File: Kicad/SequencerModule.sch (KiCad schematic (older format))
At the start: 13 parts, among them U1 L78L05_SOT89, U2 MCP4822, U4 TL072

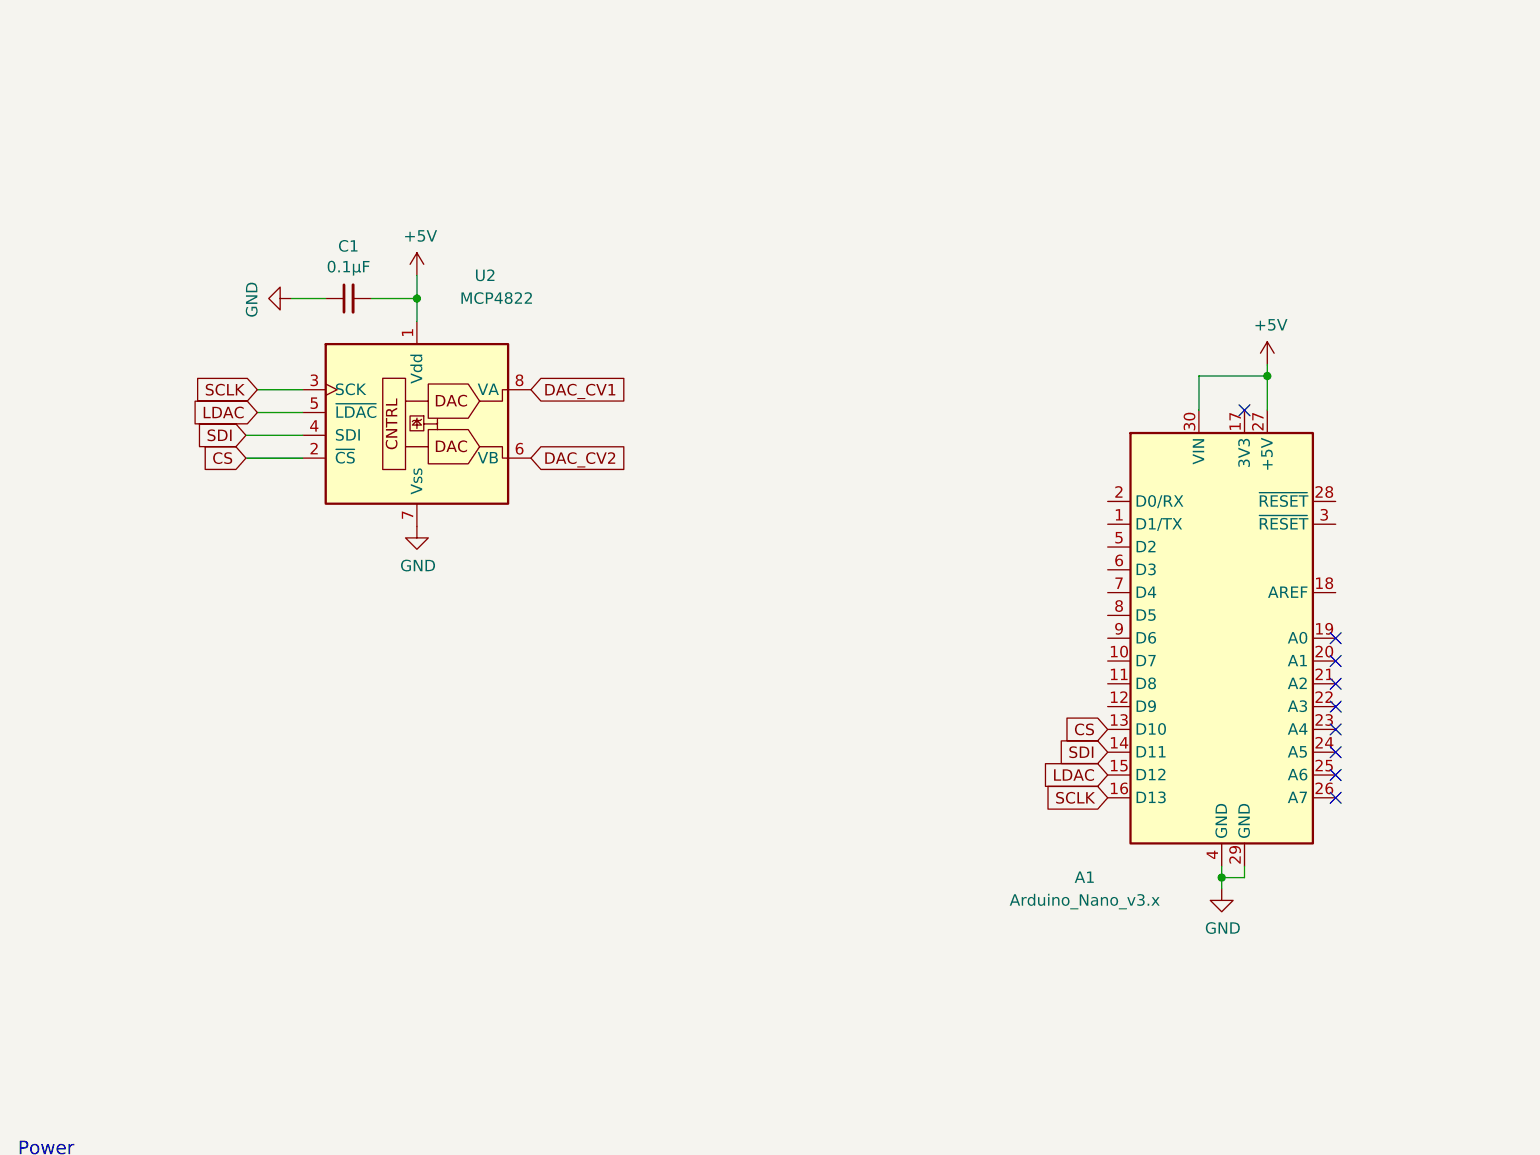
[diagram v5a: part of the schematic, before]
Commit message: switching for stm32F401, bye AtMega
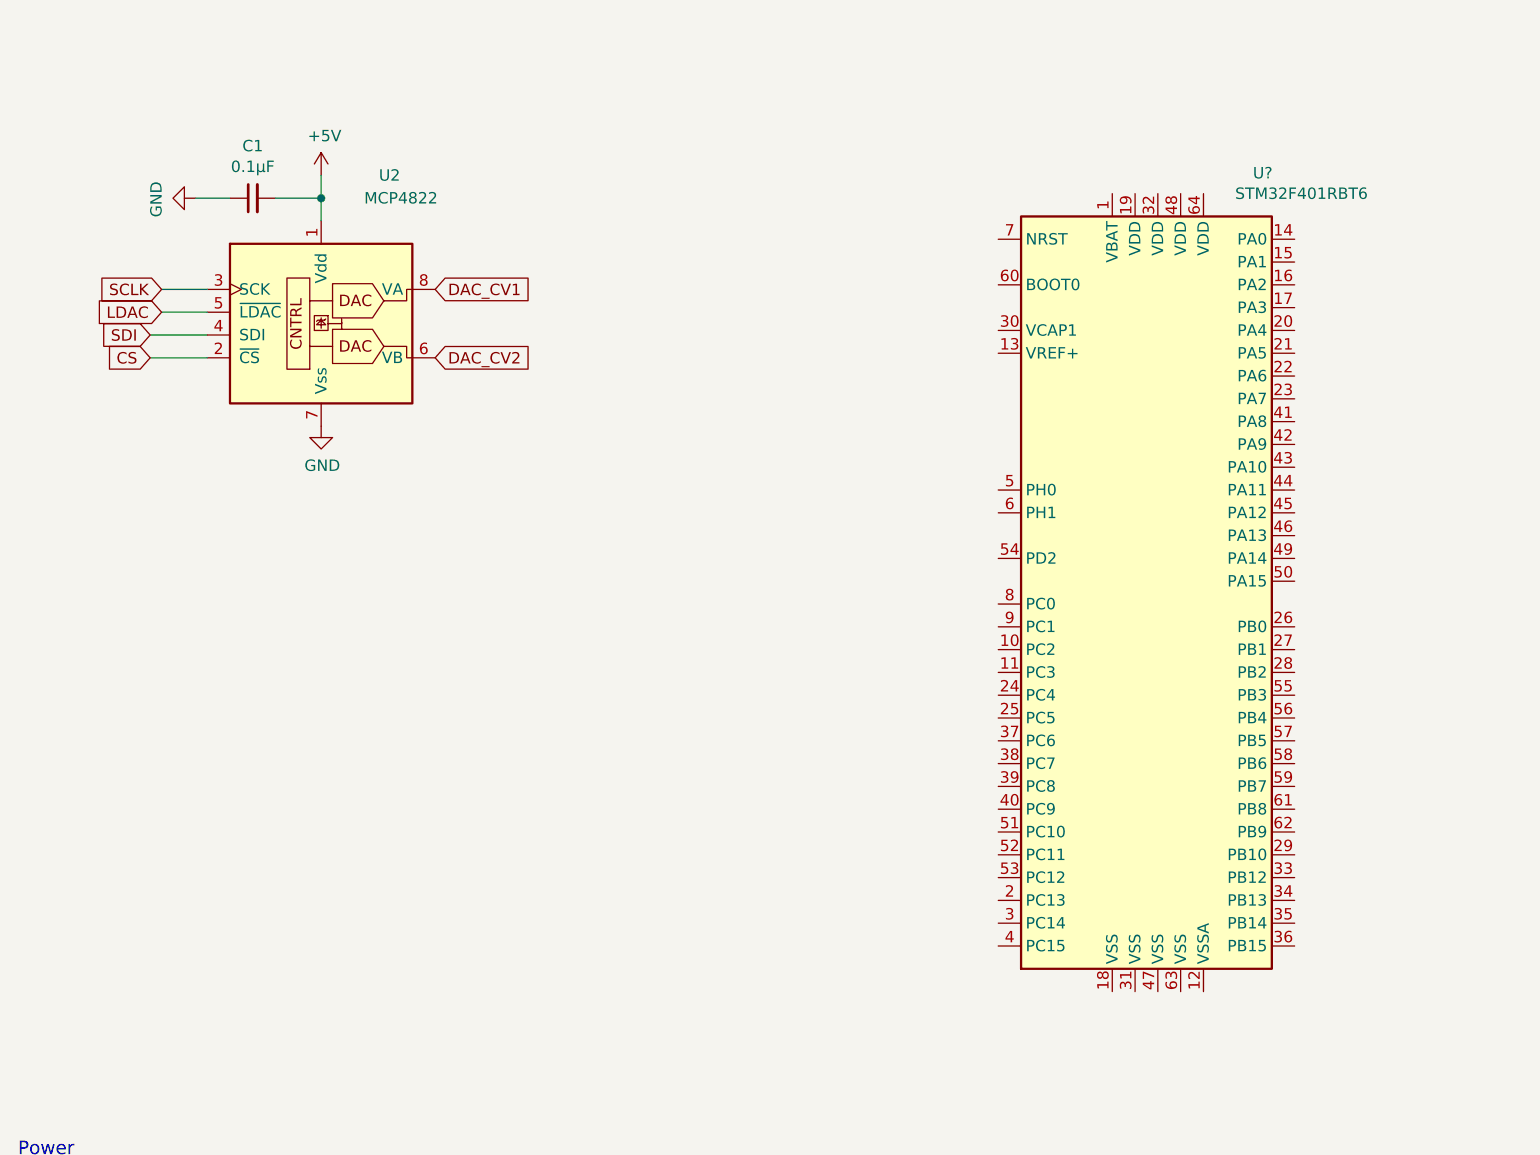
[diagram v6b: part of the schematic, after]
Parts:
- removed A1: Arduino_Nano_v3.x, Module:Arduino_Nano, symbol MCU_Module:Arduino_Nano_v3.x
- added U?: STM32F401RBT6, Package_QFP:LQFP-64_10x10mm_P0.5mm, symbol MCU_ST_STM32F4:STM32F401RBTx
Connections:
- no-connect marks 9 -> 0
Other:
- moved on the sheet: C1, U2
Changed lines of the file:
@@
 L Analog_DAC:MCP4822 U2
 U 1 1 5FAC40C6
-P 2600 2630
-F 0 "U2" H 2900 3230 50  0000 C CNN
-F 1 "MCP4822" H 2950 3130 50  0000 C CNN
-F 2 "" H 3400 2330 50  0001 C CNN
-F 3 "http://ww1.microchip.com/downloads/en/DeviceDoc/20002249B.pdf" H 3400 2330 50  0001 C CNN
-	1    2600 2630
+P 2180 2190
+F 0 "U2" H 2480 2790 50  0000 C CNN
+F 1 "MCP4822" H 2530 2690 50  0000 C CNN
+F 2 "" H 2980 1890 50  0001 C CNN
+F 3 "http://ww1.microchip.com/downloads/en/DeviceDoc/20002249B.pdf" H 2980 1890 50  0001 C CNN
+	1    2180 2190
 	1    0    0    -1
 $EndComp
@@
 L power:GND #PWR0101
 U 1 1 5FAC5967
-P 2600 3130
-F 0 "#PWR0101" H 2600 2880 50  0001 C CNN
-F 1 "GND" H 2605 2957 50  0000 C CNN
-F 2 "" H 2600 3130 50  0001 C CNN
-F 3 "" H 2600 3130 50  0001 C CNN
-	1    2600 3130
+P 2180 2690
+F 0 "#PWR0101" H 2180 2440 50  0001 C CNN
+F 1 "GND" H 2185 2517 50  0000 C CNN
+F 2 "" H 2180 2690 50  0001 C CNN
+F 3 "" H 2180 2690 50  0001 C CNN
+	1    2180 2690
 	1    0    0    -1
 $EndComp
@@
 L Device:C_Small C1
 U 1 1 5FAC8AF5
-P 2300 2130
-F 0 "C1" V 2529 2130 50  0000 C CNN
-F 1 "0.1μF" V 2438 2130 50  0000 C CNN
-F 2 "" H 2300 2130 50  0001 C CNN
-F 3 "~" H 2300 2130 50  0001 C CNN
-	1    2300 2130
+P 1880 1690
+F 0 "C1" V 2109 1690 50  0000 C CNN
+F 1 "0.1μF" V 2018 1690 50  0000 C CNN
+F 2 "" H 1880 1690 50  0001 C CNN
+F 3 "~" H 1880 1690 50  0001 C CNN
+	1    1880 1690
 	0    -1   -1   0
 $EndComp
 Wire Wire Line
-	2600 2030 2600 2130
-Wire Wire Line
-	2400 2130 2600 2130
-Connection ~ 2600 2130
-Wire Wire Line
-	2600 2130 2600 2230
+	2180 1590 2180 1690
+Wire Wire Line
+	1980 1690 2180 1690
+Connection ~ 2180 1690
+Wire Wire Line
+	2180 1690 2180 1790
 $Comp
 L power:GND #PWR0102
 U 1 1 5FAC9D1B
-P 2050 2130
-F 0 "#PWR0102" H 2050 1880 50  0001 C CNN
-F 1 "GND" H 2055 1957 50  0000 C CNN
-F 2 "" H 2050 2130 50  0001 C CNN
-F 3 "" H 2050 2130 50  0001 C CNN
-	1    2050 2130
+P 1630 1690
+F 0 "#PWR0102" H 1630 1440 50  0001 C CNN
+F 1 "GND" H 1635 1517 50  0000 C CNN
+F 2 "" H 1630 1690 50  0001 C CNN
+F 3 "" H 1630 1690 50  0001 C CNN
+	1    1630 1690
 	0    1    1    0
 $EndComp
 Wire Wire Line
-	2050 2130 2200 2130
-Text GLabel 1900 2530 0    50   Input ~ 0
+	1630 1690 1780 1690
+Text GLabel 1480 2090 0    50   Input ~ 0
 SCLK
-Text GLabel 1850 2830 0    50   Input ~ 0
+Text GLabel 1430 2390 0    50   Input ~ 0
 CS
-Text GLabel 3100 2530 2    50   Input ~ 0
+Text GLabel 2680 2090 2    50   Input ~ 0
 DAC_CV1
-Text GLabel 3100 2830 2    50   Input ~ 0
+Text GLabel 2680 2390 2    50   Input ~ 0
 DAC_CV2
 Wire Wire Line
-	1900 2530 2100 2530
-Wire Wire Line
-	1900 2630 2100 2630
-Wire Wire Line
-	1850 2730 2100 2730
-Wire Wire Line
-	1850 2830 2100 2830
-$Comp
-L MCU_Module:Arduino_Nano_v3.x A1
-U 1 1 5FAD0791
-P 6130 3620
-F 0 "A1" H 5530 2570 50  0000 C CNN
-F 1 "Arduino_Nano_v3.x" H 5530 2470 50  0000 C CNN
-F 2 "Module:Arduino_Nano" H 6130 3620 50  0001 C CIN
-F 3 "http://www.mouser.com/pdfdocs/Gravitech_Arduino_Nano3_0.pdf" H 6130 3620 50  0001 C CNN
-	1    6130 3620
-	1    0    0    -1
-$EndComp
-$Comp
-L power:GND #PWR0103
-U 1 1 5FAD2D29
-P 6130 4720
-F 0 "#PWR0103" H 6130 4470 50  0001 C CNN
-F 1 "GND" H 6135 4547 50  0000 C CNN
-F 2 "" H 6130 4720 50  0001 C CNN
-F 3 "" H 6130 4720 50  0001 C CNN
-	1    6130 4720
-	1    0    0    -1
-$EndComp
-Wire Wire Line
-	6130 4620 6130 4670
-Wire Wire Line
-	6230 4620 6230 4670
-Wire Wire Line
-	6230 4670 6130 4670
-Connection ~ 6130 4670
-Wire Wire Line
-	6130 4670 6130 4720
-Text GLabel 5630 4120 0    50   Input ~ 0
+	1480 2090 1680 2090
+Wire Wire Line
+	1480 2190 1680 2190
+Wire Wire Line
+	1430 2290 1680 2290
+Wire Wire Line
+	1430 2390 1680 2390
+Text GLabel 1430 2290 0    50   Input ~ 0
 SDI
-Text GLabel 1850 2730 0    50   Input ~ 0
-SDI
-Text GLabel 5630 4320 0    50   Input ~ 0
-SCLK
 $Comp
 L Device:D_Small D2
@@
 L power:+5V #PWR0110
 U 1 1 5FB4B6EF
-P 2600 2030
-F 0 "#PWR0110" H 2600 1880 50  0001 C CNN
-F 1 "+5V" H 2615 2203 50  0000 C CNN
-F 2 "" H 2600 2030 50  0001 C CNN
-F 3 "" H 2600 2030 50  0001 C CNN
-	1    2600 2030
-	1    0    0    -1
-$EndComp
-$Comp
-L power:+5V #PWR0113
-U 1 1 5FB529CE
-P 6330 2420
-F 0 "#PWR0113" H 6330 2270 50  0001 C CNN
-F 1 "+5V" H 6345 2593 50  0000 C CNN
-F 2 "" H 6330 2420 50  0001 C CNN
-F 3 "" H 6330 2420 50  0001 C CNN
-	1    6330 2420
-	1    0    0    -1
-$EndComp
-Wire Wire Line
-	6330 2420 6330 2470
-Wire Wire Line
-	6030 2620 6030 2470
-Wire Wire Line
-	6030 2470 6330 2470
-Text GLabel 5630 4020 0    50   Input ~ 0
-CS
+P 2180 1590
+F 0 "#PWR0110" H 2180 1440 50  0001 C CNN
+F 1 "+5V" H 2195 1763 50  0000 C CNN
+F 2 "" H 2180 1590 50  0001 C CNN
+F 3 "" H 2180 1590 50  0001 C CNN
+	1    2180 1590
+	1    0    0    -1
+$EndComp
 $Comp
 L eurorack_custom:urorack_EURO_PWR_2x5 JP1
@@
 Wire Wire Line
 	10090 2770 10160 2770
-NoConn ~ 6230 2620
-Text GLabel 1900 2630 0    50   Input ~ 0
+Text GLabel 1480 2190 0    50   Input ~ 0
 LDAC
-Text GLabel 5630 4220 0    50   Input ~ 0
-LDAC
-NoConn ~ 6630 3620
-NoConn ~ 6630 3720
-NoConn ~ 6630 3820
-NoConn ~ 6630 3920
-NoConn ~ 6630 4020
-NoConn ~ 6630 4120
-NoConn ~ 6630 4220
-NoConn ~ 6630 4320
 $Comp
 L power:PWR_FLAG #FLG0101
@@
 	1550 6400 2450 6400
 Connection ~ 2450 6400
-Wire Wire Line
-	6330 2620 6330 2470
-Connection ~ 6330 2470
+$Comp
+L MCU_ST_STM32F4:STM32F401RBTx U?
+U 1 1 5FCBFD96
+P 5850 3370
+F 0 "U?" H 6310 5160 50  0000 C CNN
+F 1 "STM32F401RBT6" H 6480 5070 50  0000 C CNN
+F 2 "Package_QFP:LQFP-64_10x10mm_P0.5mm" H 5250 1670 50  0001 R CNN
+F 3 "http://www.st.com/st-web-ui/static/active/en/resource/technical/document/datasheet/DM00086815.pdf" H 5850 3370 50  0001 C CNN
+	1    5850 3370
+	1    0    0    -1
+$EndComp
 $EndSCHEMATC
